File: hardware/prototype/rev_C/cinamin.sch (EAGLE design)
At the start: 14 parts, among them Q3 MOSFET-NCHANNELXFDN-3, U1 AP4400_3.4_2.3, X1 16Mhz

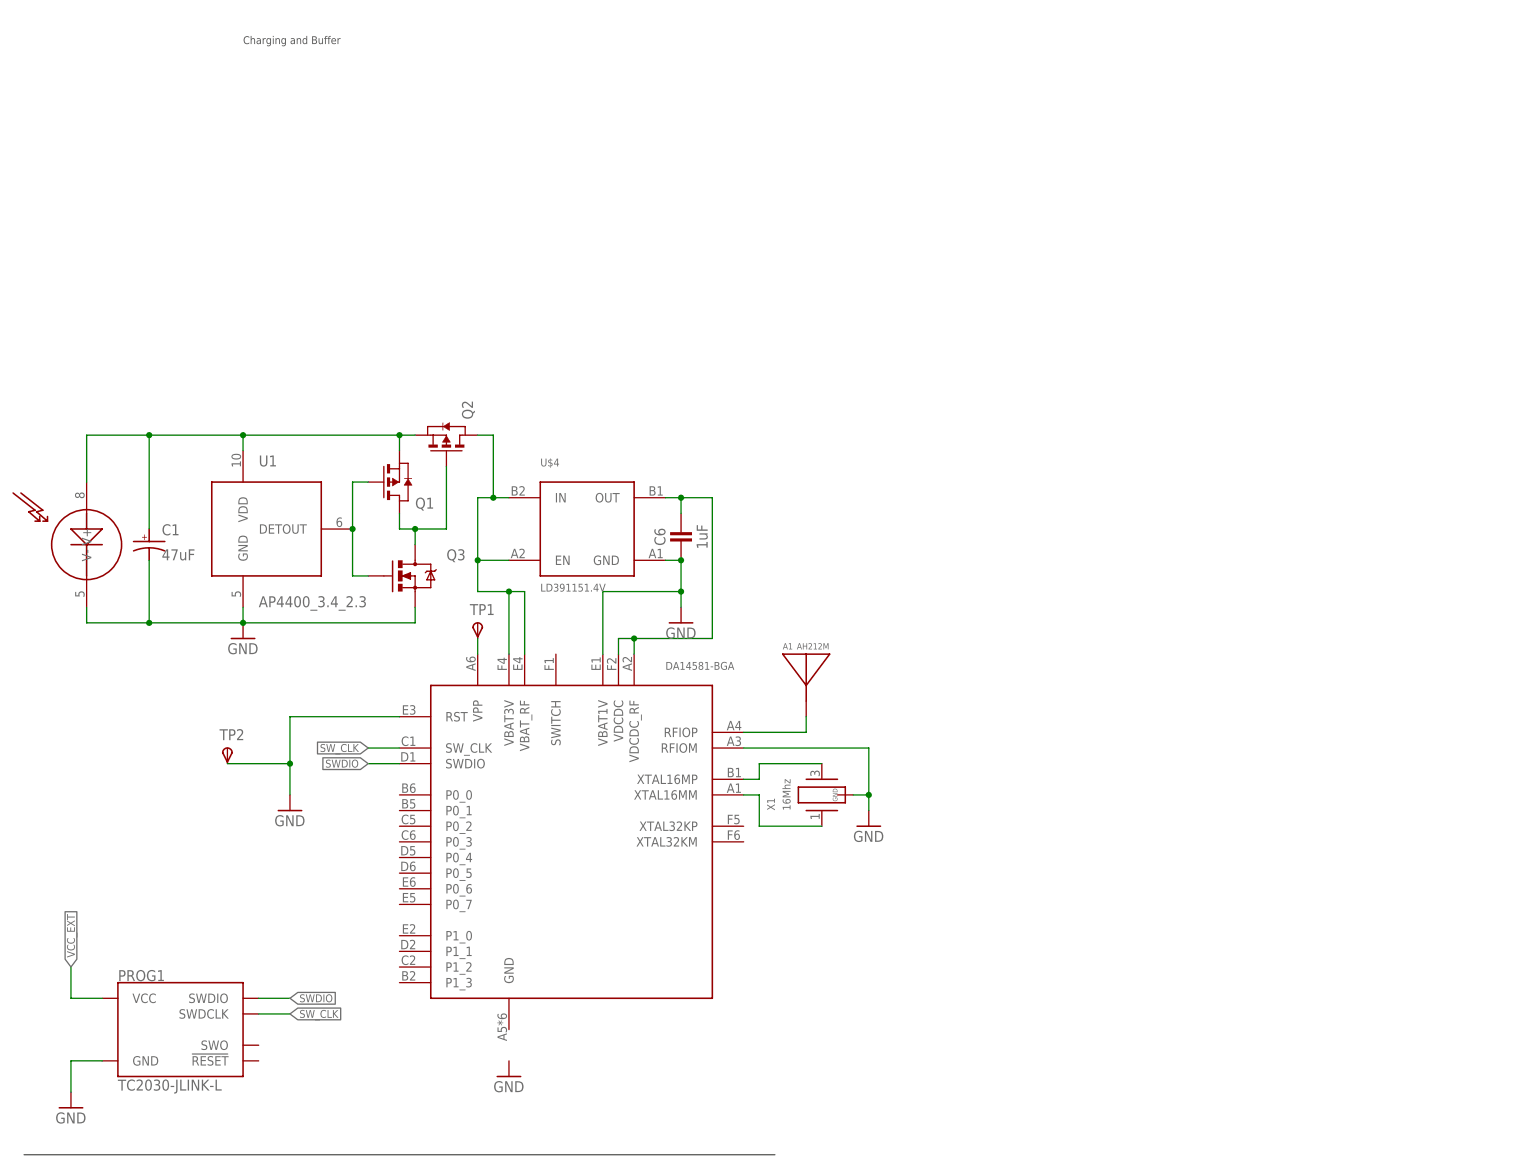
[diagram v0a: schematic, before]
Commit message: changed the revand the new prototype to include the transistor switch
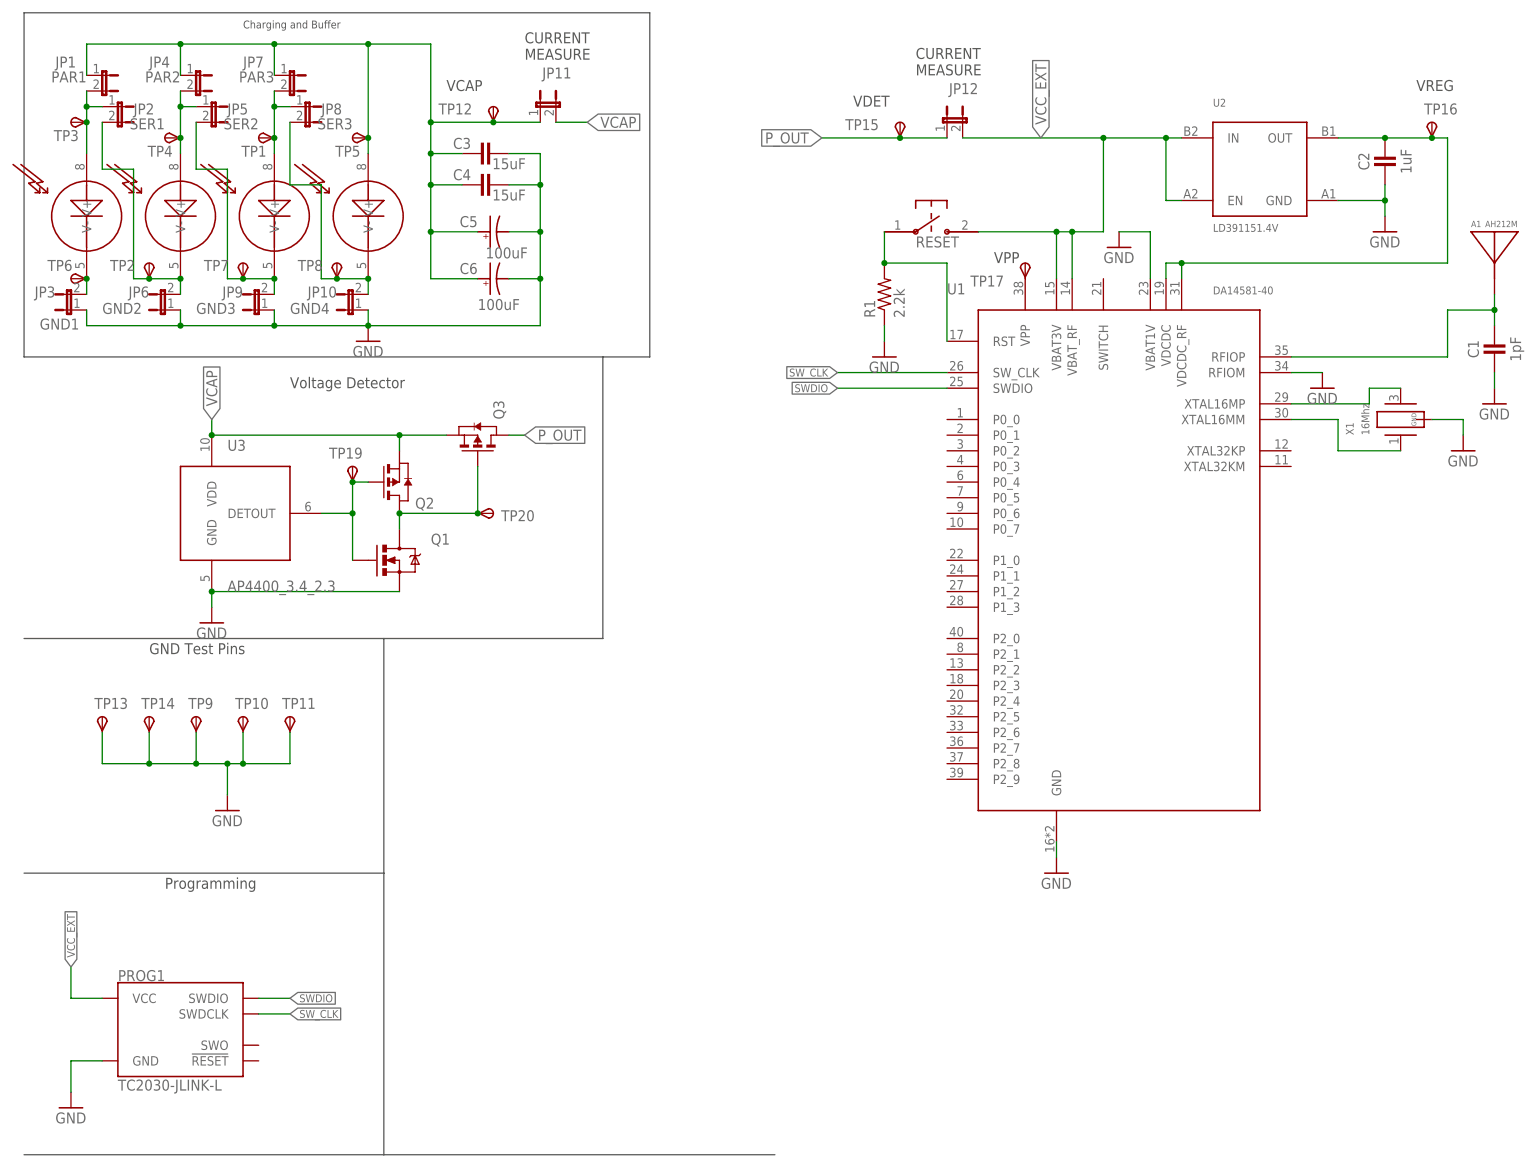
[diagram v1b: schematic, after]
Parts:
- removed U$3: DA14581-BGA, chips:DA14581-BGA
- removed U$4: LD391151.4V, chips:LD391151.4V
- added C2: 1uF, passives:CAPACITOR
- added C3, C4: 15uF, passives:CAPACITOR
- added C5: 100uF, passives:CAP_POL0603
- added D2, D3, D4: CPC1822, chips:CPC1822
- added JP1: PAR1, SparkFun-Passives:JUMPER-2PTH
- added JP10: GND4, SparkFun-Passives:JUMPER-2PTH
- added JP11: CURRENT_MEASURE1, SparkFun-Passives:JUMPER-2PTH
- added JP12: CURRENT_MEASURE2, SparkFun-Passives:JUMPER-2PTH
- added JP2: SER1, SparkFun-Passives:JUMPER-2PTH
- added JP3: GND1, SparkFun-Passives:JUMPER-2PTH
- added JP4: PAR2, SparkFun-Passives:JUMPER-2PTH
- added JP5: SER2, SparkFun-Passives:JUMPER-2PTH
- added JP6: GND2, SparkFun-Passives:JUMPER-2PTH
- added JP7: PAR3, SparkFun-Passives:JUMPER-2PTH
- added JP8: SER3, SparkFun-Passives:JUMPER-2PTH
- added JP9: GND3, SparkFun-Passives:JUMPER-2PTH
- added R1: 2.2k, passives:RESISTOR0402_RES
- added RESET: B3U-1000P, switches:B3U-1000P
- added TP10, TP11, TP13, TP14, TP9: GND, testpad:TPSPAD1-13
- added TP12, TP19, TP20: VCAP, testpad:TPSPAD1-13
- added TP15: VDET, testpad:TPSPAD1-13
- added TP16: VREG, testpad:TPSPAD1-13
- added TP17: VPP, testpad:TPSPAD1-13
- added TP3: D1H, testpad:TPSPAD1-13
- added TP4: D2H, testpad:TPSPAD1-13
- added TP5: D4H, testpad:TPSPAD1-13
- added TP6: D1L, testpad:TPSPAD1-13
- added TP7: D3L, testpad:TPSPAD1-13
- added TP8: D4L, testpad:TPSPAD1-13
- added U2: LD391151.4V, chips:LD391151.4V
- added U3: AP4400_3.4_2.3, chips:AP4400
- C1: value 47uF -> 1pF; device passives:CAP_POL0603_SMALL -> passives:CAPACITOR
- C6: value 1uF -> 100uF; device passives:CAPACITOR -> passives:CAP_POL0603
- Q1: value (none) -> MOSFET-NCHANNELXFDN-3; device fets:MOSFET-PCHANNEL -> fets:MOSFET-NCHANNELXFDN-3
- Q3: value MOSFET-NCHANNELXFDN-3 -> (none); device fets:MOSFET-NCHANNELXFDN-3 -> fets:MOSFET-PCHANNEL
- TP1: value TPSPAD1-13 -> D3H
- TP2: value TPSPAD1-13 -> D2L
- U1: value AP4400_3.4_2.3 -> DA14581-40; device chips:AP4400 -> chips:DA14581-40
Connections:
- removed net N$5: U$3.XTAL16MP, X1.2
- removed net N$7: U$3.XTAL16MM, X1.1
- removed net N$8: A1.ANTENNA, U$3.RFIOP
- removed net OUT: C6.1, U$3.VDCDC, U$3.VDCDC_RF, U$4.OUT
- removed net VCC: Q2.D, U$3.VBAT3V, U$3.VBAT_RF, U$4.EN, U$4.IN
- new net DET_OUT: Q1.G, Q2.G, TP19.PP, U3.DETOUT
- new net JP10: D4.V-, JP10.2, JP8.2, TP8.PP
- new net N$15: U1.XTAL16MP, X1.2
- new net N$18: U1.XTAL16MM, X1.1
- new net N$19: A1.ANTENNA, C1.1, U1.RFIOP
- new net N$22: R1.2, RESET.P$1, U1.RST
- new net N$61: D1.V-, JP3.2, TP6.PP
- new net N$62: D2.V-, JP2.2, JP6.2, TP2.PP
- new net N$63: D3.V-, JP5.2, JP9.2, TP7.PP
- new net N$65: D1.V+, JP1.2, JP2.1, TP3.PP
- new net N$67: D2.V+, JP4.2, JP5.1, TP4.PP
- new net N$68: D3.V+, JP7.2, JP8.1, TP1.PP
- new net P_OUT: JP12.1, Q3.D, TP15.PP
- new net VCAP: JP11.2, Q2.S, Q3.S, U3.VDD
- net GND: now also C1.2, C2.2, C3.2, C4.2, C5.ANODE, C6.ANODE, JP10.1, JP3.1, JP6.1, JP9.1, Q1.S, R1.1, TP10.PP, TP11.PP, TP13.PP, TP14.PP, TP9.PP, U1.RFIOM, U1.VBAT1V, U2.GND, U3.GND; no longer C1.ANODE, C6.2, D1.V-, Q3.S, TP2.PP, U$3.RFIOM, U$3.RST, U$3.VBAT1V, U$4.GND
- net N$1: now also C3.1, C4.1, C5.CATHODE, C6.CATHODE, D4.V+, JP1.1, JP11.1, JP4.1, JP7.1, TP12.PP, TP5.PP; no longer TP1.PP, U$3.VPP
- net N$2: now also TP17.PP, U1.VPP; no longer Q1.G, Q3.G, U1.DETOUT
- net N$3: now also C2.1, TP16.PP, U1.VDCDC, U1.VDCDC_RF, U2.OUT; no longer C1.CATHODE, D1.V+, Q1.S, Q2.S, U1.VDD
- net N$4: now also Q2.D, Q3.G, TP20.PP; no longer Q2.G, Q3.D
- net SWDIO: now also U1.SWDIO; no longer U$3.SWDIO
- net SW_CLK: now also U1.SW_CLK; no longer U$3.SW_CLK
- net VCC_EXT: now also JP12.2, RESET.P$2, U1.VBAT3V, U1.VBAT_RF, U2.EN, U2.IN
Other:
- note added: "CURRENT MEASURE"
- note added: "GND Test Pins"
- note added: "Programming"
- note added: "VCAP"
- note added: "VDET"
- note added: "VPP"
- note added: "VREG"
- note added: "Voltage Detector"
- moved on the sheet: A1, Q2, TP1, TP2, X1
